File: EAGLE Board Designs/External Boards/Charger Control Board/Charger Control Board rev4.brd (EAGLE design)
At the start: 81 parts

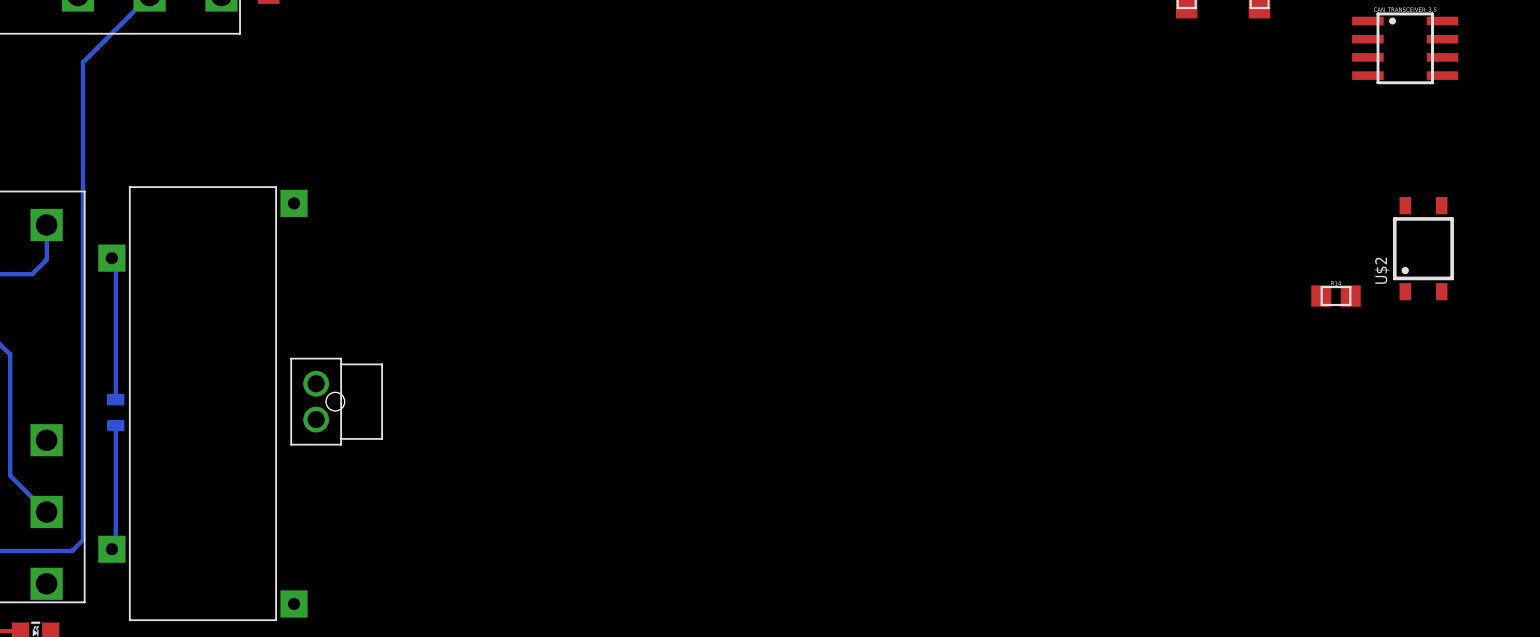
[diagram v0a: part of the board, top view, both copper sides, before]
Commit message: Flipped relay coil direction
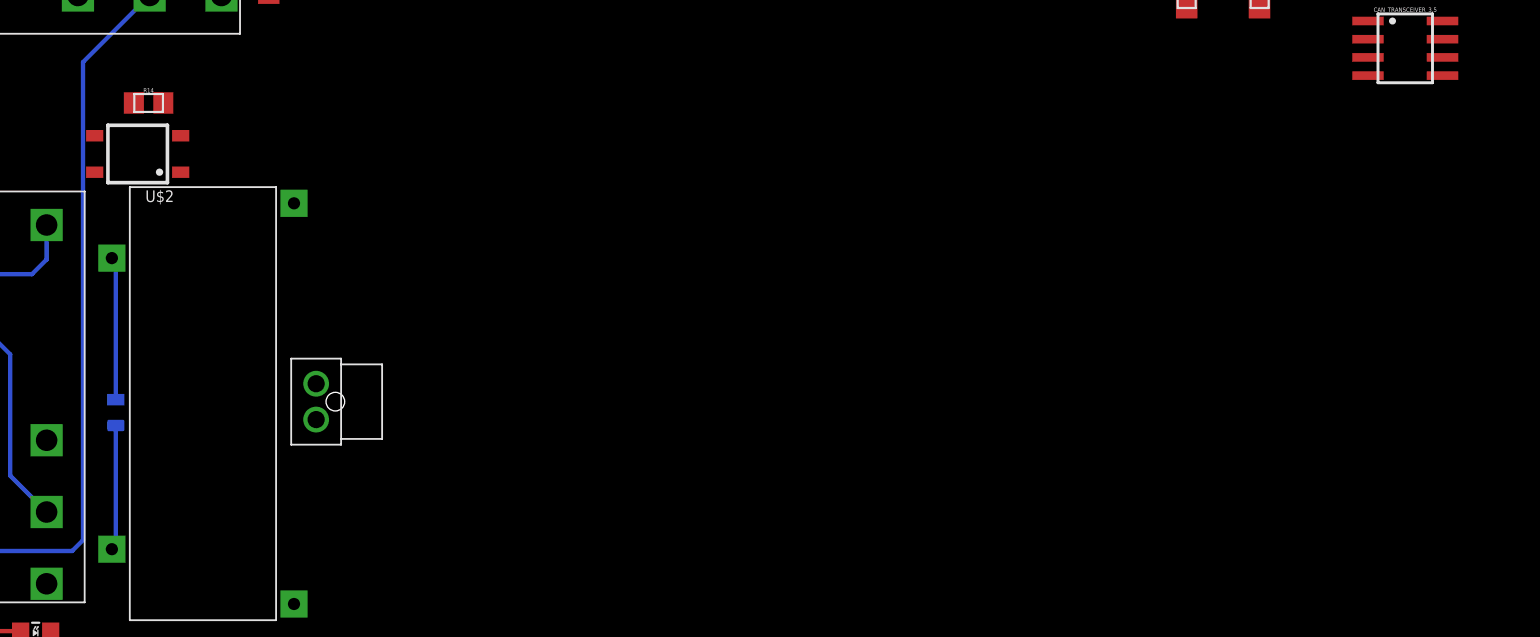
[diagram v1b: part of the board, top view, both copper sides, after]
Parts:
- moved U$2 89.9 mm to (-18.5, 56.1), turned to 90 degrees
- moved R14 83.9 mm to (-17.8, 59.7)
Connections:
- net CHARGE_CONTROL: now also U$3.C2; no longer U$3.C1
- net GND: now also U$3.C1; no longer U$3.C2
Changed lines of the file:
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@@
 <attribute name="VALUE" x="-65.786" y="50.3428" size="0.3048" layer="27" align="top-center"/>
 </element>
-<element name="R14" library="HyTechDevices" package="0805" value="360" x="65.024" y="46.228" smashed="yes">
-<attribute name="NAME" x="65.024" y="46.9519" size="0.3048" layer="25" align="bottom-center"/>
-<attribute name="TOLERANCE" value="1%" x="65.024" y="46.228" size="1.778" layer="27" display="off"/>
-<attribute name="VALUE" x="65.024" y="45.5168" size="0.3048" layer="27" align="top-center"/>
+<element name="R14" library="HyTechDevices" package="0805" value="360" x="-17.78" y="59.69" smashed="yes">
+<attribute name="NAME" x="-17.78" y="60.4139" size="0.3048" layer="25" align="bottom-center"/>
+<attribute name="TOLERANCE" value="1%" x="-17.78" y="59.69" size="1.778" layer="27" display="off"/>
+<attribute name="VALUE" x="-17.78" y="58.9788" size="0.3048" layer="27" align="top-center"/>
 </element>
 <element name="R15" library="HyTechDevices" package="0805" value="68" x="71.12" y="69.85" smashed="yes" rot="R90">
@@
 <attribute name="VALUE" x="-75.311" y="57.531" size="0.3048" layer="28" rot="MR0" align="bottom-center"/>
 </element>
-<element name="U$2" library="HyTechDevices" package="SOP04" value="CPC1002N" x="71.12" y="49.53" smashed="yes">
-<attribute name="NAME" x="68.58" y="46.99" size="0.8128" layer="25" rot="R90"/>
-<attribute name="VALUE" x="74.93" y="46.99" size="1.27" layer="27" rot="R90"/>
+<element name="U$2" library="HyTechDevices" package="SOP04" value="CPC1002N" x="-18.542" y="56.134" smashed="yes" rot="R90">
+<attribute name="NAME" x="-16.002" y="53.594" size="0.8128" layer="25" rot="R180"/>
+<attribute name="VALUE" x="-16.002" y="59.944" size="1.27" layer="27" rot="R180"/>
 </element>
 <element name="U$4" library="HyTechDevices" package="TEENSY_3.2_SIMPLE" value="TEENSY_3.2_SIMPLE" x="-41.91" y="64.516" smashed="yes" rot="R90"/>
@@
 <contactref element="MAIN" pad="P$3"/>
 <contactref element="D3" pad="A"/>
-<contactref element="U$3" pad="C2"/>
 <contactref element="CAN_TRANSCEIVER_3.5" pad="8"/>
 <contactref element="CAN_TRANSCEIVER_3.5" pad="2"/>
@@
 <contactref element="R31" pad="2"/>
 <wire x1="-20.066" y1="39" x2="-20.066" y2="48.598" width="0.3048" layer="16"/>
-<wire x1="-20.066" y1="48.598" x2="-20.34" y2="48.872" width="0.3048" layer="16"/>
+<contactref element="U$3" pad="C1"/>
 <wire x1="68.58" y1="78.52" x2="78.74" y2="78.52" width="0" layer="19" extent="1-1"/>
 <wire x1="68.58" y1="70.9" x2="68.58" y2="78.52" width="0" layer="19" extent="1-1"/>
@@
 <wire x1="59.69" y1="68.335" x2="67.25" y2="64.135" width="0" layer="19" extent="1-1"/>
 <wire x1="54.61" y1="68.335" x2="59.69" y2="68.335" width="0" layer="19" extent="1-1"/>
-<wire x1="72.39" y1="46.53" x2="67.25" y2="64.135" width="0" layer="19" extent="1-1"/>
 <wire x1="-9.398" y1="74.964" x2="54.61" y2="68.335" width="0" layer="19" extent="1-1"/>
-<wire x1="-30.718" y1="71.562" x2="-9.398" y2="74.964" width="0" layer="19" extent="1-16"/>
-<wire x1="-33.528" y1="71.637" x2="-30.718" y2="71.562" width="0" layer="19" extent="16-16"/>
-<wire x1="-38.542" y1="71.612" x2="-33.528" y2="71.637" width="0" layer="19" extent="16-16"/>
-<wire x1="-57.658" y1="73.415" x2="-38.542" y2="71.612" width="0" layer="19" extent="16-16"/>
-<wire x1="-59.944" y1="73.415" x2="-57.658" y2="73.415" width="0" layer="19" extent="16-16"/>
-<wire x1="-62.805" y1="72.39" x2="-59.944" y2="73.415" width="0" layer="19" extent="16-16"/>
-<wire x1="-68.005" y1="73.66" x2="-62.805" y2="72.39" width="0" layer="19" extent="16-16"/>
-<wire x1="-76.2" y1="65.786" x2="-68.005" y2="73.66" width="0" layer="19" extent="16-16"/>
-<wire x1="-77.127" y1="61.178" x2="-76.2" y2="65.786" width="0" layer="19" extent="1-1"/>
-<wire x1="-73.914" y1="57.642" x2="-77.127" y2="61.178" width="0" layer="19" extent="1-16"/>
+<wire x1="-15.542" y1="57.404" x2="-9.398" y2="74.964" width="0" layer="19" extent="1-1"/>
+<wire x1="-20.066" y1="48.598" x2="-15.542" y2="57.404" width="0" layer="19" extent="1-16"/>
+<wire x1="-20.34" y1="28.572" x2="-20.066" y2="39" width="0" layer="19" extent="16-16"/>
+<wire x1="-24.892" y1="26.162" x2="-20.34" y2="28.572" width="0" layer="19" extent="1-1"/>
+<wire x1="-24.604" y1="22.86" x2="-24.892" y2="26.162" width="0" layer="19" extent="1-1"/>
+<wire x1="-30.471" y1="42.418" x2="-20.066" y2="39" width="0" layer="19" extent="16-16"/>
+<wire x1="-39.082" y1="22.86" x2="-24.604" y2="22.86" width="0" layer="19" extent="1-1"/>
+<wire x1="-39.37" y1="26.162" x2="-39.082" y2="22.86" width="0" layer="19" extent="1-1"/>
+<wire x1="-45.711" y1="41.402" x2="-30.471" y2="42.418" width="0" layer="19" extent="16-16"/>
+<wire x1="-56.368" y1="29.21" x2="-45.711" y2="41.402" width="0" layer="19" extent="16-16"/>
+<wire x1="-64.77" y1="27.686" x2="-56.368" y2="29.21" width="0" layer="19" extent="1-1"/>
+<wire x1="-71.44" y1="33.544" x2="-64.77" y2="27.686" width="0" layer="19" extent="1-1"/>
+<wire x1="-73.34" y1="36.846" x2="-71.44" y2="33.544" width="0" layer="19" extent="1-1"/>
+<wire x1="-75.175" y1="34.798" x2="-73.34" y2="36.846" width="0" layer="19" extent="1-1"/>
+<wire x1="-74.93" y1="44.47" x2="-73.34" y2="36.846" width="0" layer="19" extent="1-1"/>
+<wire x1="-73.914" y1="57.642" x2="-74.93" y2="44.47" width="0" layer="19" extent="16-16"/>
+<wire x1="-77.127" y1="61.178" x2="-73.914" y2="57.642" width="0" layer="19" extent="1-16"/>
+<wire x1="-76.2" y1="65.786" x2="-77.127" y2="61.178" width="0" layer="19" extent="1-1"/>
 <wire x1="-69.177" y1="61.178" x2="-73.914" y2="57.642" width="0" layer="19" extent="1-16"/>
 <wire x1="-67.818" y1="57.921" x2="-69.177" y2="61.178" width="0" layer="19" extent="1-16"/>
@@
 <wire x1="-60.164" y1="53.594" x2="-60.164" y2="60.452" width="0" layer="19" extent="1-1"/>
 <wire x1="-60.164" y1="51.054" x2="-60.164" y2="53.594" width="0" layer="19" extent="1-1"/>
-<wire x1="-74.93" y1="44.47" x2="-73.914" y2="57.642" width="0" layer="19" extent="16-16"/>
-<wire x1="-73.34" y1="36.846" x2="-74.93" y2="44.47" width="0" layer="19" extent="1-1"/>
-<wire x1="-75.175" y1="34.798" x2="-73.34" y2="36.846" width="0" layer="19" extent="1-1"/>
-<wire x1="-71.44" y1="33.544" x2="-73.34" y2="36.846" width="0" layer="19" extent="1-1"/>
-<wire x1="-64.77" y1="27.686" x2="-71.44" y2="33.544" width="0" layer="19" extent="1-1"/>
-<wire x1="-56.368" y1="29.21" x2="-64.77" y2="27.686" width="0" layer="19" extent="1-1"/>
+<wire x1="-68.005" y1="73.66" x2="-76.2" y2="65.786" width="0" layer="19" extent="16-16"/>
+<wire x1="-62.805" y1="72.39" x2="-68.005" y2="73.66" width="0" layer="19" extent="16-16"/>
+<wire x1="-59.944" y1="73.415" x2="-62.805" y2="72.39" width="0" layer="19" extent="16-16"/>
+<wire x1="-57.658" y1="73.415" x2="-59.944" y2="73.415" width="0" layer="19" extent="16-16"/>
 <wire x1="-76.2" y1="84.836" x2="-68.005" y2="73.66" width="0" layer="19" extent="16-16"/>
-<wire x1="-45.711" y1="41.402" x2="-56.368" y2="29.21" width="0" layer="19" extent="16-16"/>
-<wire x1="-30.471" y1="42.418" x2="-45.711" y2="41.402" width="0" layer="19" extent="16-16"/>
-<wire x1="-20.066" y1="39" x2="-30.471" y2="42.418" width="0" layer="19" extent="16-16"/>
-<wire x1="-24.892" y1="26.162" x2="-20.066" y2="39" width="0" layer="19" extent="16-16"/>
-<wire x1="-24.604" y1="22.86" x2="-24.892" y2="26.162" width="0" layer="19" extent="1-1"/>
-<wire x1="-39.082" y1="22.86" x2="-24.604" y2="22.86" width="0" layer="19" extent="1-1"/>
-<wire x1="-39.37" y1="26.162" x2="-39.082" y2="22.86" width="0" layer="19" extent="1-1"/>
+<wire x1="-38.542" y1="71.612" x2="-57.658" y2="73.415" width="0" layer="19" extent="16-16"/>
+<wire x1="-33.528" y1="71.637" x2="-38.542" y2="71.612" width="0" layer="19" extent="16-16"/>
+<wire x1="-30.718" y1="71.562" x2="-33.528" y2="71.637" width="0" layer="19" extent="16-16"/>
 <wire x1="-49.276" y1="93.989" x2="-57.658" y2="73.415" width="0" layer="19" extent="1-16"/>
 <wire x1="-10.16" y1="134.865" x2="-49.276" y2="93.989" width="0" layer="19" extent="1-1"/>
@@
 <contactref element="U$2" pad="1"/>
 <contactref element="R14" pad="2"/>
-<wire x1="66.049" y1="46.228" x2="69.85" y2="46.53" width="0" layer="19" extent="1-1"/>
+<wire x1="-15.542" y1="54.864" x2="-16.755" y2="59.69" width="0" layer="19" extent="1-1"/>
 </signal>
 <signal name="TOGGLE_CHARGER">
 <contactref element="R14" pad="1"/>
 <contactref element="U$4" pad="D11"/>
-<wire x1="-45.72" y1="65.786" x2="63.999" y2="46.228" width="0" layer="19" extent="1-1"/>
+<wire x1="-45.72" y1="65.786" x2="-18.805" y2="59.69" width="0" layer="19" extent="1-1"/>
 </signal>
 <signal name="CHARGE_CONTROL">
 <contactref element="U$2" pad="3"/>
-<contactref element="U$3" pad="C1"/>
 <contactref element="D3" pad="C"/>
 <wire x1="-20.066" y1="37.2" x2="-20.066" y2="28.846" width="0.3048" layer="16"/>
-<wire x1="-20.066" y1="28.846" x2="-20.34" y2="28.572" width="0.3048" layer="16"/>
-<wire x1="-20.066" y1="37.2" x2="72.39" y2="52.53" width="0" layer="19" extent="1-16"/>
+<contactref element="U$3" pad="C2"/>
+<wire x1="-20.34" y1="48.872" x2="-21.542" y2="57.404" width="0" layer="19" extent="1-1"/>
+<wire x1="-20.066" y1="37.2" x2="-20.34" y2="48.872" width="0" layer="19" extent="16-16"/>
 </signal>
 <signal name="+5V">
@@
 <wire x1="-26.913" y1="73.787" x2="-10.16" y2="136.915" width="0" layer="19" extent="1-16"/>
 <wire x1="-60.452" y1="42.672" x2="-26.162" y2="71.383" width="0" layer="19" extent="1-16"/>
-<wire x1="69.85" y1="52.53" x2="-26.162" y2="71.383" width="0" layer="19" extent="1-16"/>
+<wire x1="-21.542" y1="54.864" x2="-26.162" y2="71.383" width="0" layer="19" extent="1-16"/>
 </signal>
 <signal name="N$8">
